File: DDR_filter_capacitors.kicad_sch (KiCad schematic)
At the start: 25 parts

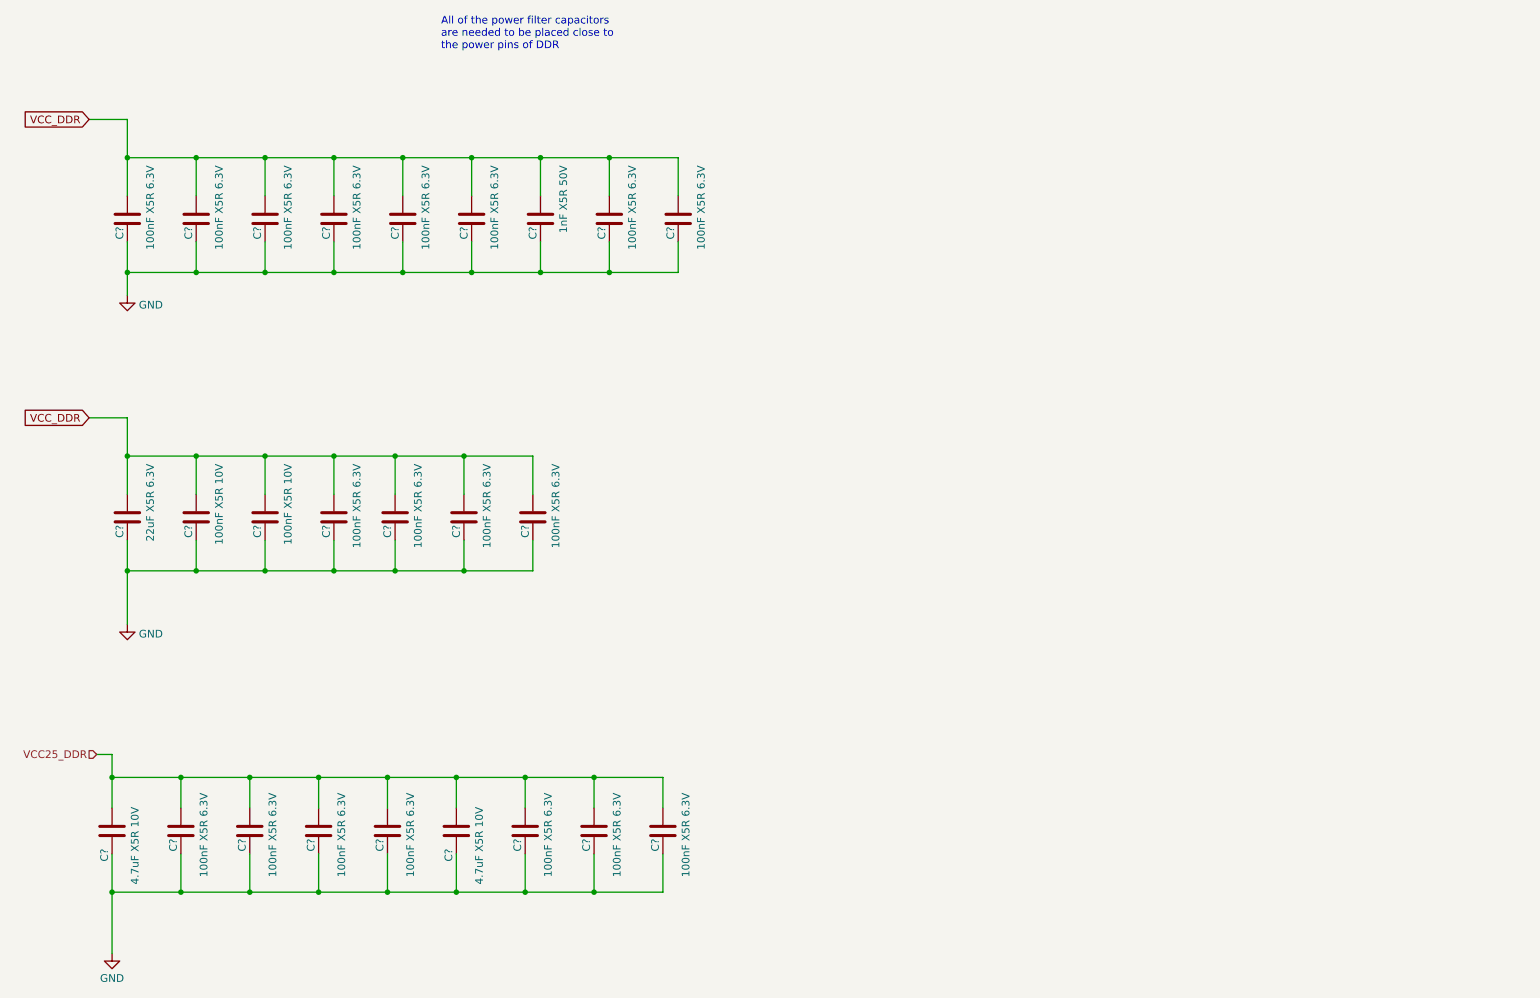
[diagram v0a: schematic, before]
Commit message: added more capacitors for second DDR4
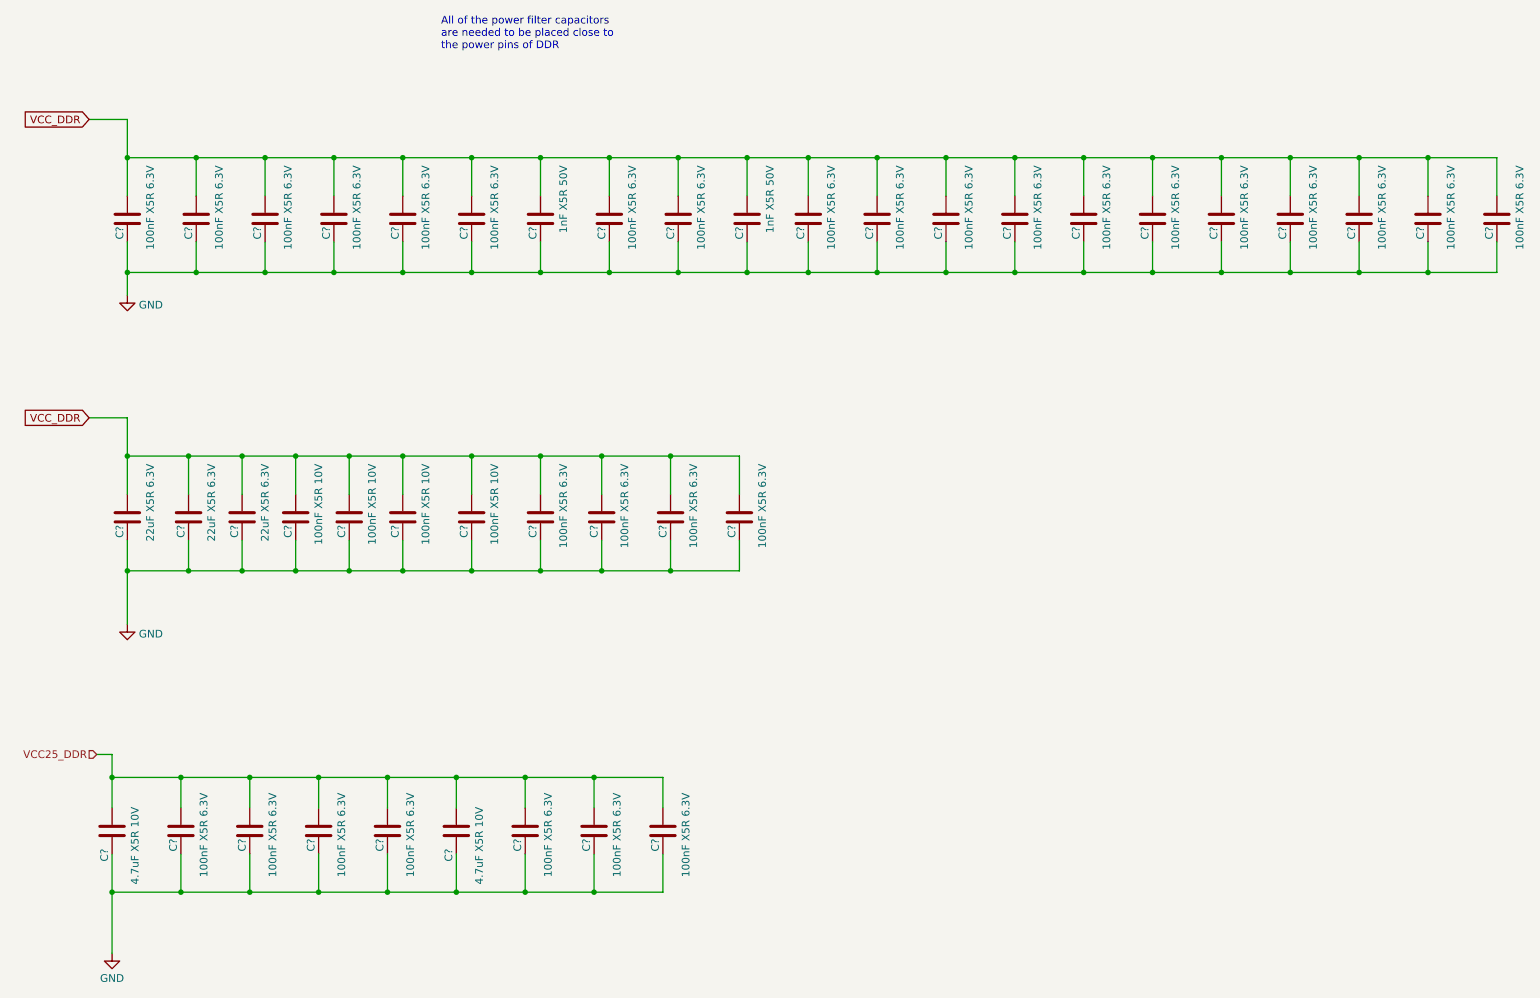
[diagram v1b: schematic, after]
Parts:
- added C? (x11): 100nF X5R 6.3V, Capacitor_SMD:C_0201_0603Metric, symbol Device:C
- added C? (x2): 22uF X5R 6.3V, Capacitor_SMD:C_0603_1608Metric, symbol Device:C
- added C?: 1nF X5R 50V, Capacitor_SMD:C_0402_1005Metric, symbol Device:C
- added C? (x2): 100nF X5R 10V, Capacitor_SMD:C_0402_1005Metric, symbol Device:C
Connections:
- net GND: now also C?.1, C?.1, C?.1, C?.1, C?.1, C?.1, C?.1, C?.1, C?.1, C?.1, C?.1, C?.1, C?.1, C?.1, C?.1, C?.1
- net VCC_DDR: now also C?.2, C?.2, C?.2, C?.2, C?.2, C?.2, C?.2, C?.2, C?.2, C?.2, C?.2, C?.2, C?.2, C?.2, C?.2, C?.2
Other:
- moved on the sheet: C?

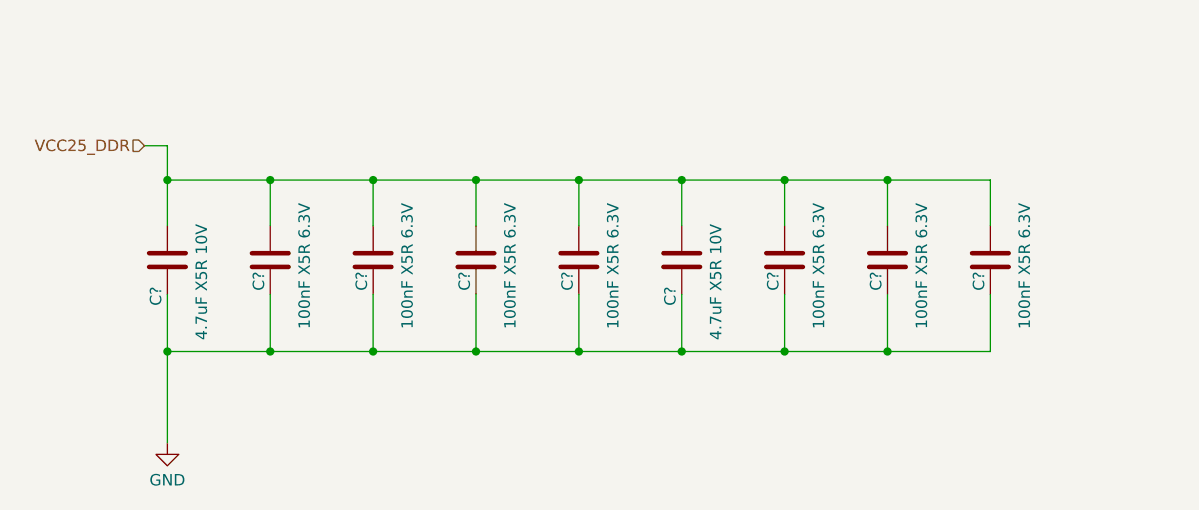
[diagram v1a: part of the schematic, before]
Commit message: placed DDR Capacitors
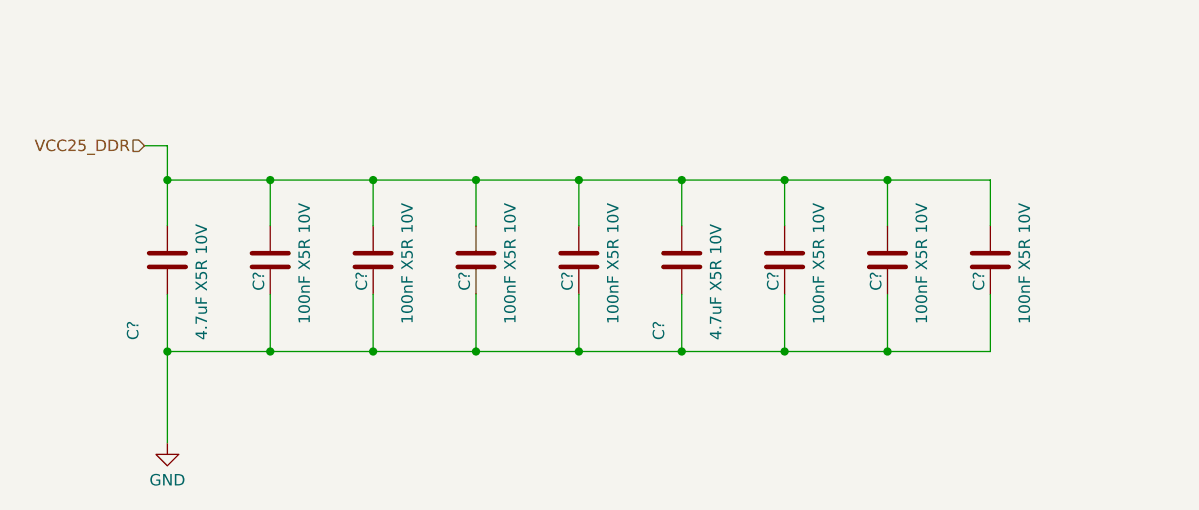
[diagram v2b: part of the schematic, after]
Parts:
- C? (x7): value 100nF X5R 6.3V -> 100nF X5R 10V; footprint Capacitor_SMD:C_0201_0603Metric -> Capacitor_SMD:C_0402_1005Metric; LCSC C76928 -> C76934; Model GRM033R60J104KE19D -> GRM033R61A104KE15D
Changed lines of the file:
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@@
       (effects (font (size 1.27 1.27)) (justify left))
     )
-    (property "Value" "100nF X5R 6.3V" (at 63.5 149.86 90)
-      (effects (font (size 1.27 1.27)) (justify left))
-    )
-    (property "Footprint" "Capacitor_SMD:C_0201_0603Metric" (at 58.7248 152.4 0)
+    (property "Value" "100nF X5R 10V" (at 63.5 149.86 90)
+      (effects (font (size 1.27 1.27)) (justify left))
+    )
+    (property "Footprint" "Capacitor_SMD:C_0402_1005Metric" (at 58.7248 152.4 0)
       (effects (font (size 1.27 1.27)) hide)
     )
@@
       (effects (font (size 1.27 1.27)) hide)
     )
-    (property "Description" "容值: 100nF 精度: ±10% 额定电压: 6.3V 材质(温度系数): X5R 材质:X5R" (at 59.69 156.21 0)
-      (effects (font (size 1.27 1.27)) hide)
-    )
-    (property "LCSC" "C76928" (at 59.69 156.21 0)
-      (effects (font (size 1.27 1.27)) hide)
-    )
-    (property "Model" "GRM033R60J104KE19D" (at 59.69 156.21 0)
+    (property "Description" "容值: 100nF 精度: ±10% 额定电压: 10V 材质(温度系数): X5R 材质:X5R" (at 59.69 156.21 0)
+      (effects (font (size 1.27 1.27)) hide)
+    )
+    (property "LCSC" "C76934" (at 59.69 156.21 0)
+      (effects (font (size 1.27 1.27)) hide)
+    )
+    (property "Model" "GRM033R61A104KE15D" (at 59.69 156.21 0)
       (effects (font (size 1.27 1.27)) hide)
     )
@@
       (effects (font (size 1.27 1.27)) (justify left))
     )
-    (property "Value" "100nF X5R 6.3V" (at 74.93 149.86 90)
-      (effects (font (size 1.27 1.27)) (justify left))
-    )
-    (property "Footprint" "Capacitor_SMD:C_0201_0603Metric" (at 70.1548 152.4 0)
+    (property "Value" "100nF X5R 10V" (at 74.93 149.86 90)
+      (effects (font (size 1.27 1.27)) (justify left))
+    )
+    (property "Footprint" "Capacitor_SMD:C_0402_1005Metric" (at 70.1548 152.4 0)
       (effects (font (size 1.27 1.27)) hide)
     )
@@
       (effects (font (size 1.27 1.27)) hide)
     )
-    (property "Description" "容值: 100nF 精度: ±10% 额定电压: 6.3V 材质(温度系数): X5R 材质:X5R" (at 71.12 156.21 0)
-      (effects (font (size 1.27 1.27)) hide)
-    )
-    (property "LCSC" "C76928" (at 71.12 156.21 0)
-      (effects (font (size 1.27 1.27)) hide)
-    )
-    (property "Model" "GRM033R60J104KE19D" (at 71.12 156.21 0)
+    (property "Description" "容值: 100nF 精度: ±10% 额定电压: 10V 材质(温度系数): X5R 材质:X5R" (at 71.12 156.21 0)
+      (effects (font (size 1.27 1.27)) hide)
+    )
+    (property "LCSC" "C76934" (at 71.12 156.21 0)
+      (effects (font (size 1.27 1.27)) hide)
+    )
+    (property "Model" "GRM033R61A104KE15D" (at 71.12 156.21 0)
       (effects (font (size 1.27 1.27)) hide)
     )
@@
       (effects (font (size 1.27 1.27)) (justify left))
     )
-    (property "Value" "100nF X5R 6.3V" (at 109.22 149.86 90)
-      (effects (font (size 1.27 1.27)) (justify left))
-    )
-    (property "Footprint" "Capacitor_SMD:C_0201_0603Metric" (at 104.4448 152.4 0)
+    (property "Value" "100nF X5R 10V" (at 109.22 149.86 90)
+      (effects (font (size 1.27 1.27)) (justify left))
+    )
+    (property "Footprint" "Capacitor_SMD:C_0402_1005Metric" (at 104.4448 152.4 0)
       (effects (font (size 1.27 1.27)) hide)
     )
@@
       (effects (font (size 1.27 1.27)) hide)
     )
-    (property "Description" "容值: 100nF 精度: ±10% 额定电压: 6.3V 材质(温度系数): X5R 材质:X5R" (at 105.41 156.21 0)
-      (effects (font (size 1.27 1.27)) hide)
-    )
-    (property "LCSC" "C76928" (at 105.41 156.21 0)
-      (effects (font (size 1.27 1.27)) hide)
-    )
-    (property "Model" "GRM033R60J104KE19D" (at 105.41 156.21 0)
+    (property "Description" "容值: 100nF 精度: ±10% 额定电压: 10V 材质(温度系数): X5R 材质:X5R" (at 105.41 156.21 0)
+      (effects (font (size 1.27 1.27)) hide)
+    )
+    (property "LCSC" "C76934" (at 105.41 156.21 0)
+      (effects (font (size 1.27 1.27)) hide)
+    )
+    (property "Model" "GRM033R61A104KE15D" (at 105.41 156.21 0)
       (effects (font (size 1.27 1.27)) hide)
     )
@@
       (effects (font (size 1.27 1.27)) (justify left))
     )
-    (property "Value" "100nF X5R 6.3V" (at 52.07 149.86 90)
-      (effects (font (size 1.27 1.27)) (justify left))
-    )
-    (property "Footprint" "Capacitor_SMD:C_0201_0603Metric" (at 47.2948 152.4 0)
+    (property "Value" "100nF X5R 10V" (at 52.07 149.86 90)
+      (effects (font (size 1.27 1.27)) (justify left))
+    )
+    (property "Footprint" "Capacitor_SMD:C_0402_1005Metric" (at 47.2948 152.4 0)
       (effects (font (size 1.27 1.27)) hide)
     )
@@
       (effects (font (size 1.27 1.27)) hide)
     )
-    (property "Description" "容值: 100nF 精度: ±10% 额定电压: 6.3V 材质(温度系数): X5R 材质:X5R" (at 48.26 156.21 0)
-      (effects (font (size 1.27 1.27)) hide)
-    )
-    (property "LCSC" "C76928" (at 48.26 156.21 0)
-      (effects (font (size 1.27 1.27)) hide)
-    )
-    (property "Model" "GRM033R60J104KE19D" (at 48.26 156.21 0)
+    (property "Description" "容值: 100nF 精度: ±10% 额定电压: 10V 材质(温度系数): X5R 材质:X5R" (at 48.26 156.21 0)
+      (effects (font (size 1.27 1.27)) hide)
+    )
+    (property "LCSC" "C76934" (at 48.26 156.21 0)
+      (effects (font (size 1.27 1.27)) hide)
+    )
+    (property "Model" "GRM033R61A104KE15D" (at 48.26 156.21 0)
       (effects (font (size 1.27 1.27)) hide)
     )
@@
       (effects (font (size 1.27 1.27)) (justify left))
     )
-    (property "Value" "100nF X5R 6.3V" (at 120.65 149.86 90)
-      (effects (font (size 1.27 1.27)) (justify left))
-    )
-    (property "Footprint" "Capacitor_SMD:C_0201_0603Metric" (at 115.8748 152.4 0)
+    (property "Value" "100nF X5R 10V" (at 120.65 149.86 90)
+      (effects (font (size 1.27 1.27)) (justify left))
+    )
+    (property "Footprint" "Capacitor_SMD:C_0402_1005Metric" (at 115.8748 152.4 0)
       (effects (font (size 1.27 1.27)) hide)
     )
@@
       (effects (font (size 1.27 1.27)) hide)
     )
-    (property "Description" "容值: 100nF 精度: ±10% 额定电压: 6.3V 材质(温度系数): X5R 材质:X5R" (at 116.84 156.21 0)
-      (effects (font (size 1.27 1.27)) hide)
-    )
-    (property "LCSC" "C76928" (at 116.84 156.21 0)
-      (effects (font (size 1.27 1.27)) hide)
-    )
-    (property "Model" "GRM033R60J104KE19D" (at 116.84 156.21 0)
+    (property "Description" "容值: 100nF 精度: ±10% 额定电压: 10V 材质(温度系数): X5R 材质:X5R" (at 116.84 156.21 0)
+      (effects (font (size 1.27 1.27)) hide)
+    )
+    (property "LCSC" "C76934" (at 116.84 156.21 0)
+      (effects (font (size 1.27 1.27)) hide)
+    )
+    (property "Model" "GRM033R61A104KE15D" (at 116.84 156.21 0)
       (effects (font (size 1.27 1.27)) hide)
     )
@@
   (symbol (lib_id "Device:C") (at 93.98 156.21 0) (unit 1)
     (in_bom yes) (on_board yes) (dnp no)
-    (property "Reference" "C?" (at 92.71 161.29 90)
+    (property "Reference" "C?" (at 91.44 165.1 90)
       (effects (font (size 1.27 1.27)) (justify left))
     )
@@
       (effects (font (size 1.27 1.27)) (justify left))
     )
-    (property "Value" "100nF X5R 6.3V" (at 132.08 149.86 90)
-      (effects (font (size 1.27 1.27)) (justify left))
-    )
-    (property "Footprint" "Capacitor_SMD:C_0201_0603Metric" (at 127.3048 152.4 0)
+    (property "Value" "100nF X5R 10V" (at 132.08 149.86 90)
+      (effects (font (size 1.27 1.27)) (justify left))
+    )
+    (property "Footprint" "Capacitor_SMD:C_0402_1005Metric" (at 127.3048 152.4 0)
       (effects (font (size 1.27 1.27)) hide)
     )
@@
       (effects (font (size 1.27 1.27)) hide)
     )
-    (property "Description" "容值: 100nF 精度: ±10% 额定电压: 6.3V 材质(温度系数): X5R 材质:X5R" (at 128.27 156.21 0)
-      (effects (font (size 1.27 1.27)) hide)
-    )
-    (property "LCSC" "C76928" (at 128.27 156.21 0)
-      (effects (font (size 1.27 1.27)) hide)
-    )
-    (property "Model" "GRM033R60J104KE19D" (at 128.27 156.21 0)
+    (property "Description" "容值: 100nF 精度: ±10% 额定电压: 10V 材质(温度系数): X5R 材质:X5R" (at 128.27 156.21 0)
+      (effects (font (size 1.27 1.27)) hide)
+    )
+    (property "LCSC" "C76934" (at 128.27 156.21 0)
+      (effects (font (size 1.27 1.27)) hide)
+    )
+    (property "Model" "GRM033R61A104KE15D" (at 128.27 156.21 0)
       (effects (font (size 1.27 1.27)) hide)
     )
@@
       (effects (font (size 1.27 1.27)) (justify left))
     )
-    (property "Value" "100nF X5R 6.3V" (at 86.36 149.86 90)
-      (effects (font (size 1.27 1.27)) (justify left))
-    )
-    (property "Footprint" "Capacitor_SMD:C_0201_0603Metric" (at 81.5848 152.4 0)
+    (property "Value" "100nF X5R 10V" (at 86.36 149.86 90)
+      (effects (font (size 1.27 1.27)) (justify left))
+    )
+    (property "Footprint" "Capacitor_SMD:C_0402_1005Metric" (at 81.5848 152.4 0)
       (effects (font (size 1.27 1.27)) hide)
     )
@@
       (effects (font (size 1.27 1.27)) hide)
     )
-    (property "Description" "容值: 100nF 精度: ±10% 额定电压: 6.3V 材质(温度系数): X5R 材质:X5R" (at 82.55 156.21 0)
-      (effects (font (size 1.27 1.27)) hide)
-    )
-    (property "LCSC" "C76928" (at 82.55 156.21 0)
-      (effects (font (size 1.27 1.27)) hide)
-    )
-    (property "Model" "GRM033R60J104KE19D" (at 82.55 156.21 0)
+    (property "Description" "容值: 100nF 精度: ±10% 额定电压: 10V 材质(温度系数): X5R 材质:X5R" (at 82.55 156.21 0)
+      (effects (font (size 1.27 1.27)) hide)
+    )
+    (property "LCSC" "C76934" (at 82.55 156.21 0)
+      (effects (font (size 1.27 1.27)) hide)
+    )
+    (property "Model" "GRM033R61A104KE15D" (at 82.55 156.21 0)
       (effects (font (size 1.27 1.27)) hide)
     )
@@
   (symbol (lib_id "Device:C") (at 36.83 156.21 0) (unit 1)
     (in_bom yes) (on_board yes) (dnp no)
-    (property "Reference" "C?" (at 35.56 161.29 90)
-      (effects (font (size 1.27 1.27)) (justify left))
-    )
+    (property "Reference" "C?" (at 33.02 165.1 90)
+      (effects (font (size 1.27 1.27)) (justify left))
+    )
